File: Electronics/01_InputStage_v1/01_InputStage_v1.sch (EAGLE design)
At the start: 32 parts, among them J1 BARRIER_BLOCK-2PIN, J17 CONN_2X3_SMD, J2 BARRIER_BLOCK-2PIN, J3 BARRIER_BLOCK-2PIN, SW1 SWITCH_TABSSWITCH_TABS3, U1 XL4005-DEV, U2 DIODE_BIG

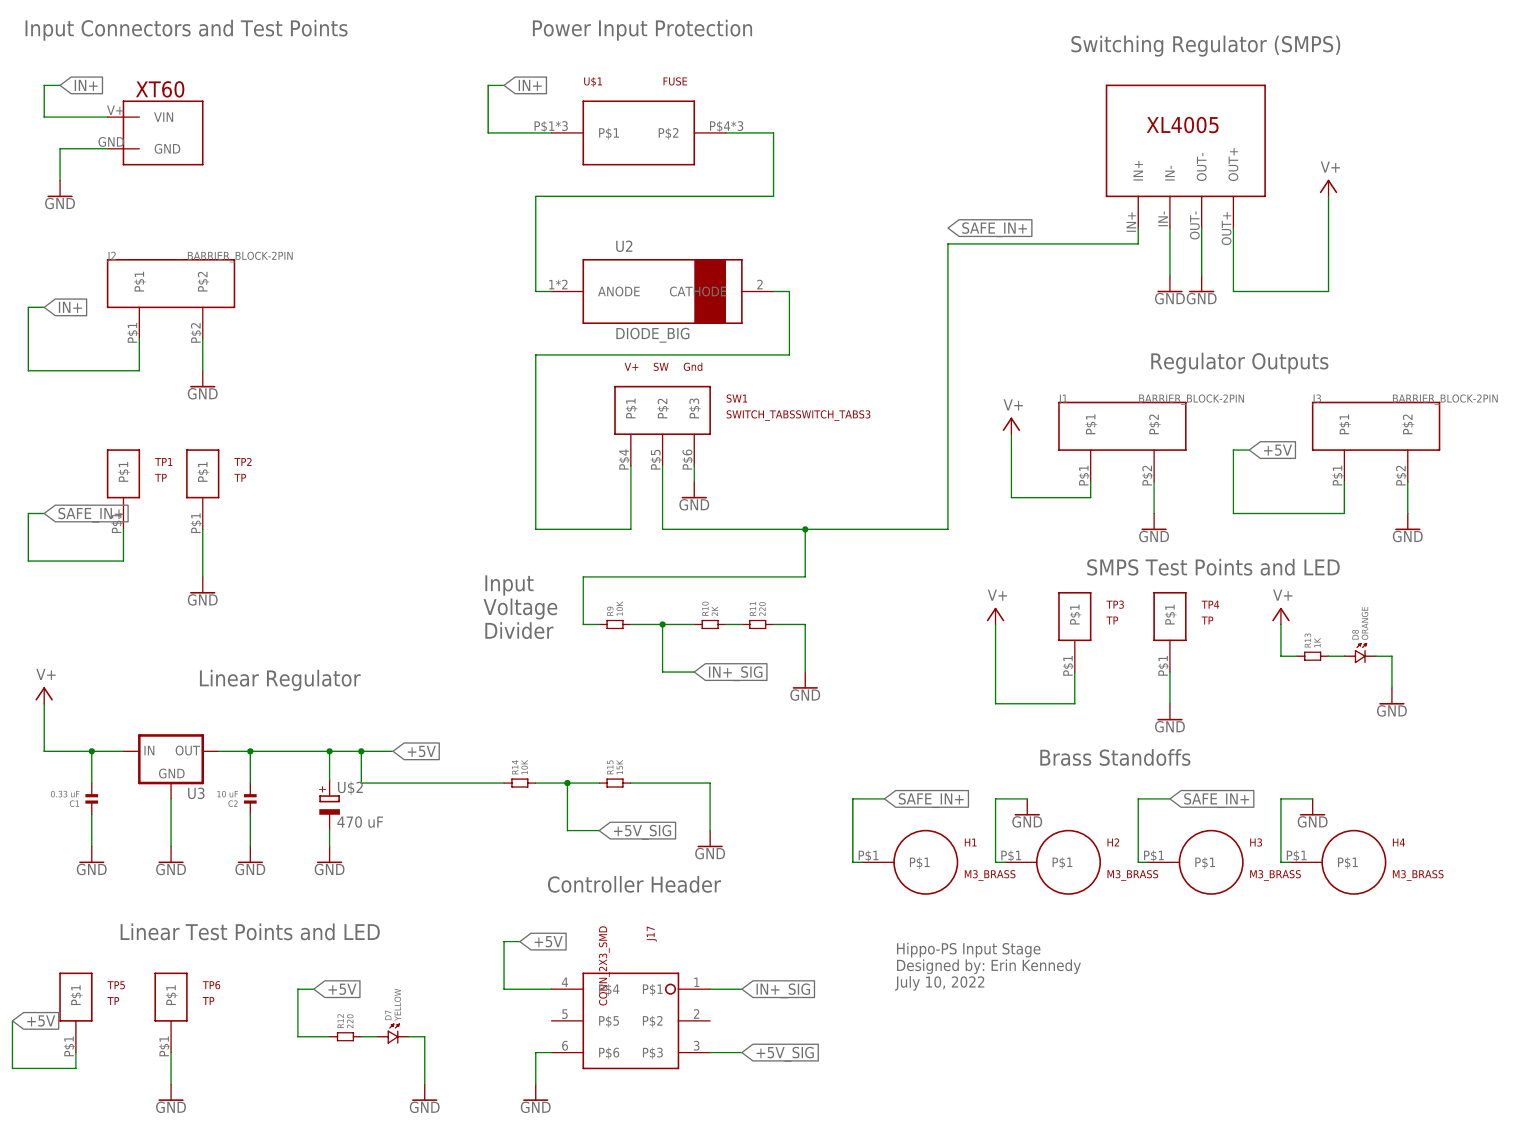
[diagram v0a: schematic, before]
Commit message: Input stage: Added PTC and moved some traces around
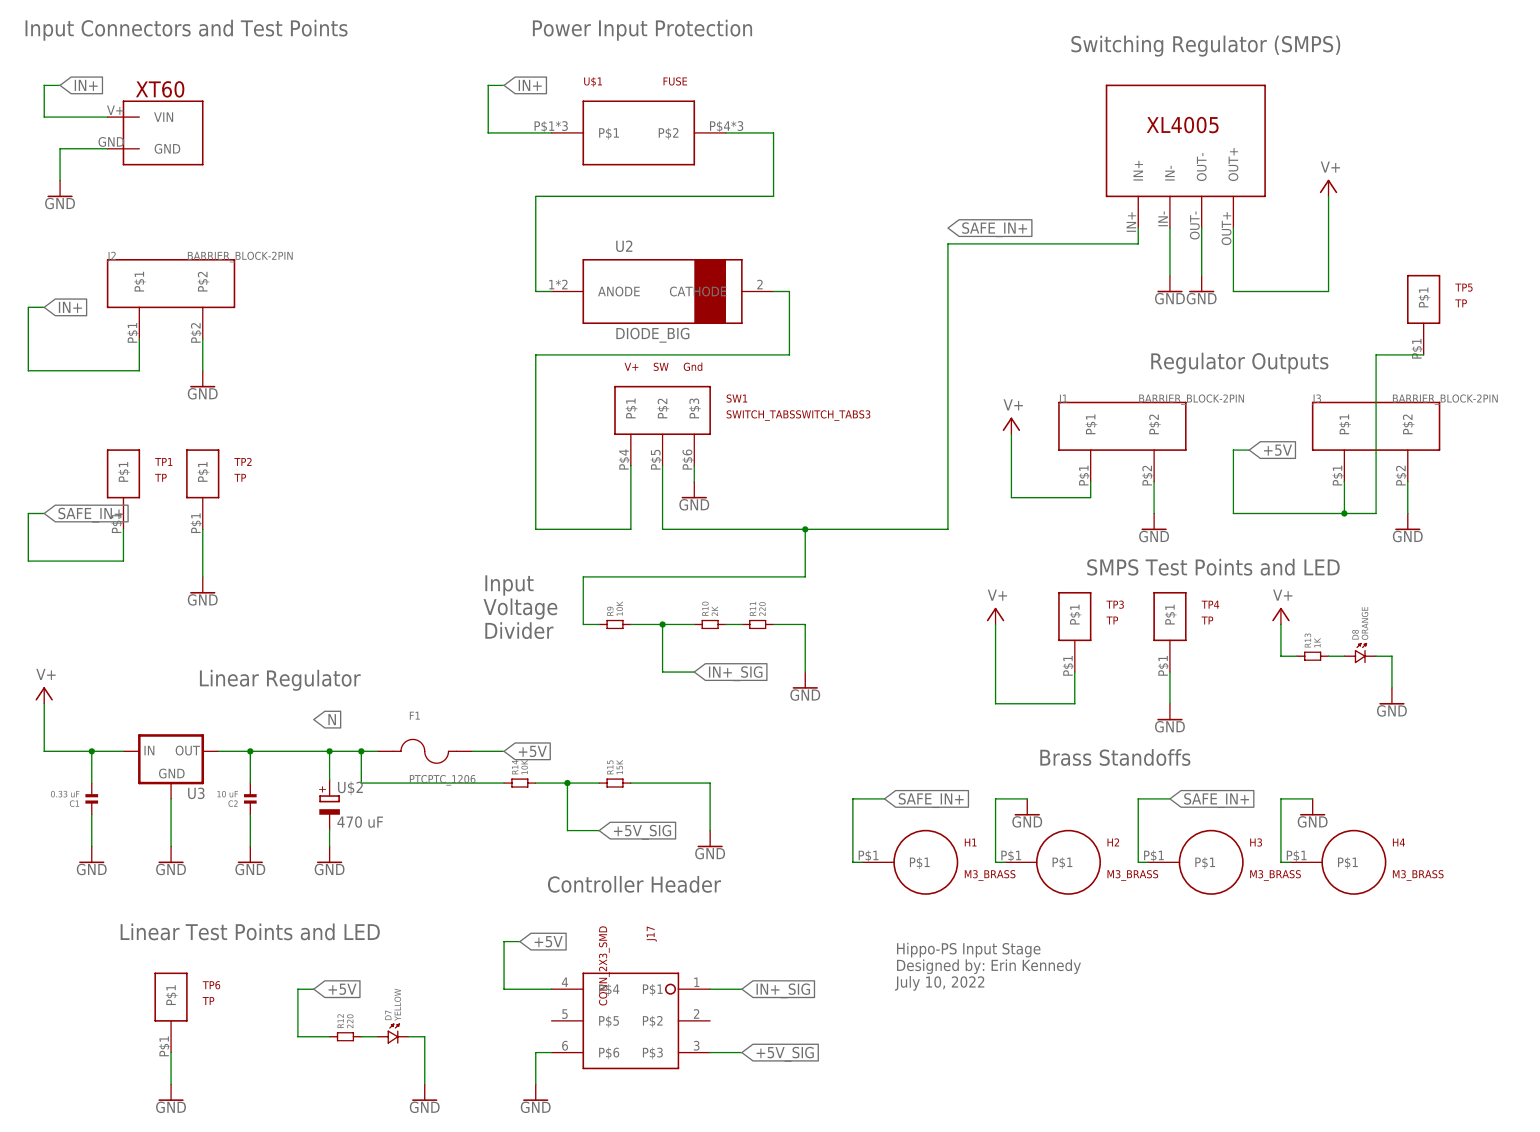
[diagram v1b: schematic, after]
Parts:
- added F1: PTCPTC_1206, Hippo-PS:PTCPTC_1206
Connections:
- new net N: C2.2, F1.1, R14.1, U$2.+, U3.OUT
- net +5V: now also F1.2; no longer C2.2, R14.1, U$2.+, U3.OUT
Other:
- moved on the sheet: TP5
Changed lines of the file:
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@@
 <part name="J3" library="Hippo-PS" deviceset="BARRIER_BLOCK-2PIN" device=""/>
 <part name="GND21" library="SparkFun-PowerSymbols" library_urn="urn:adsk.eagle:library:530" deviceset="GND" device=""/>
+<part name="F1" library="Hippo-PS" deviceset="PTC" device="PTC_1206"/>
 </parts>
 <sheets>
@@
 <attribute name="VALUE" x="218.44" y="53.086" size="1.778" layer="96" align="top-center"/>
 </instance>
-<instance part="TP5" gate="G$1" x="20.32" y="20.32" smashed="yes">
-<attribute name="NAME" x="25.4" y="25.4" size="1.27" layer="94"/>
-<attribute name="VALUE" x="25.4" y="22.86" size="1.27" layer="94"/>
+<instance part="TP5" gate="G$1" x="236.22" y="132.08" smashed="yes">
+<attribute name="NAME" x="241.3" y="137.16" size="1.27" layer="94"/>
+<attribute name="VALUE" x="241.3" y="134.62" size="1.27" layer="94"/>
 </instance>
 <instance part="TP6" gate="G$1" x="35.56" y="20.32" smashed="yes">
@@
 <instance part="GND21" gate="1" x="233.68" y="99.06" smashed="yes">
 <attribute name="VALUE" x="233.68" y="98.806" size="1.778" layer="96" align="top-center"/>
+</instance>
+<instance part="F1" gate="G$1" x="76.2" y="63.5" smashed="yes">
+<attribute name="NAME" x="73.66" y="68.58" size="1.27" layer="95"/>
+<attribute name="VALUE" x="73.66" y="58.42" size="1.27" layer="96"/>
 </instance>
 </instances>
@@
 <net name="+5V" class="0">
 <segment>
-<pinref part="U3" gate="G$1" pin="OUT"/>
-<wire x1="43.18" y1="63.5" x2="48.26" y2="63.5" width="0.1524" layer="91"/>
-<pinref part="C2" gate="G$1" pin="2"/>
-<wire x1="48.26" y1="63.5" x2="60.96" y2="63.5" width="0.1524" layer="91"/>
-<wire x1="48.26" y1="58.42" x2="48.26" y2="63.5" width="0.1524" layer="91"/>
-<junction x="48.26" y="63.5"/>
-<pinref part="U$2" gate="G$1" pin="+"/>
-<wire x1="60.96" y1="58.88" x2="60.96" y2="63.5" width="0.1524" layer="91"/>
-<junction x="60.96" y="63.5"/>
-<label x="71.12" y="63.5" size="1.778" layer="95" xref="yes"/>
-<wire x1="60.96" y1="63.5" x2="66.04" y2="63.5" width="0.1524" layer="91"/>
-<wire x1="66.04" y1="63.5" x2="71.12" y2="63.5" width="0.1524" layer="91"/>
-<wire x1="66.04" y1="63.5" x2="66.04" y2="58.42" width="0.1524" layer="91"/>
-<junction x="66.04" y="63.5"/>
-<pinref part="R14" gate="G$1" pin="1"/>
-<wire x1="66.04" y1="58.42" x2="88.9" y2="58.42" width="0.1524" layer="91"/>
-</segment>
-<segment>
-<pinref part="TP5" gate="G$1" pin="P$1"/>
-<wire x1="20.32" y1="15.24" x2="20.32" y2="12.7" width="0.1524" layer="91"/>
-<wire x1="20.32" y1="12.7" x2="10.16" y2="12.7" width="0.1524" layer="91"/>
-<wire x1="10.16" y1="12.7" x2="10.16" y2="20.32" width="0.1524" layer="91"/>
-<label x="10.16" y="20.32" size="1.778" layer="95" xref="yes"/>
-</segment>
-<segment>
 <pinref part="R12" gate="G$1" pin="1"/>
 <wire x1="60.96" y1="17.78" x2="55.88" y2="17.78" width="0.1524" layer="91"/>
@@
 </segment>
 <segment>
-<pinref part="J3" gate="G$1" pin="P$1"/>
-<wire x1="223.52" y1="106.68" x2="223.52" y2="101.6" width="0.1524" layer="91"/>
-<wire x1="223.52" y1="101.6" x2="205.74" y2="101.6" width="0.1524" layer="91"/>
 <wire x1="205.74" y1="101.6" x2="205.74" y2="111.76" width="0.1524" layer="91"/>
 <wire x1="205.74" y1="111.76" x2="208.28" y2="111.76" width="0.1524" layer="91"/>
 <label x="208.28" y="111.76" size="1.778" layer="95" xref="yes"/>
+<pinref part="J3" gate="G$1" pin="P$1"/>
+<wire x1="223.52" y1="106.68" x2="223.52" y2="101.6" width="0.1524" layer="91"/>
+<pinref part="TP5" gate="G$1" pin="P$1"/>
+<wire x1="236.22" y1="127" x2="228.6" y2="127" width="0.1524" layer="91"/>
+<wire x1="228.6" y1="127" x2="228.6" y2="101.6" width="0.1524" layer="91"/>
+<wire x1="228.6" y1="101.6" x2="223.52" y2="101.6" width="0.1524" layer="91"/>
+<junction x="223.52" y="101.6"/>
+<wire x1="205.74" y1="101.6" x2="223.52" y2="101.6" width="0.1524" layer="91"/>
+</segment>
+<segment>
+<pinref part="F1" gate="G$1" pin="2"/>
+<wire x1="83.82" y1="63.5" x2="88.9" y2="63.5" width="0.1524" layer="91"/>
+<label x="88.9" y="63.5" size="1.778" layer="95" xref="yes"/>
 </segment>
 </net>
@@
 </segment>
 </net>
+<net name="N" class="0">
+<segment>
+<pinref part="U3" gate="G$1" pin="OUT"/>
+<wire x1="43.18" y1="63.5" x2="48.26" y2="63.5" width="0.1524" layer="91"/>
+<pinref part="C2" gate="G$1" pin="2"/>
+<wire x1="48.26" y1="63.5" x2="60.96" y2="63.5" width="0.1524" layer="91"/>
+<wire x1="48.26" y1="58.42" x2="48.26" y2="63.5" width="0.1524" layer="91"/>
+<junction x="48.26" y="63.5"/>
+<pinref part="U$2" gate="G$1" pin="+"/>
+<wire x1="60.96" y1="58.88" x2="60.96" y2="63.5" width="0.1524" layer="91"/>
+<junction x="60.96" y="63.5"/>
+<wire x1="60.96" y1="63.5" x2="66.04" y2="63.5" width="0.1524" layer="91"/>
+<wire x1="66.04" y1="63.5" x2="66.04" y2="58.42" width="0.1524" layer="91"/>
+<pinref part="R14" gate="G$1" pin="1"/>
+<wire x1="66.04" y1="58.42" x2="88.9" y2="58.42" width="0.1524" layer="91"/>
+<pinref part="F1" gate="G$1" pin="1"/>
+<wire x1="68.58" y1="63.5" x2="66.04" y2="63.5" width="0.1524" layer="91"/>
+<junction x="66.04" y="63.5"/>
+<label x="58.42" y="68.58" size="1.778" layer="95" xref="yes"/>
+</segment>
+</net>

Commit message: Change fuse holder to through-hole component
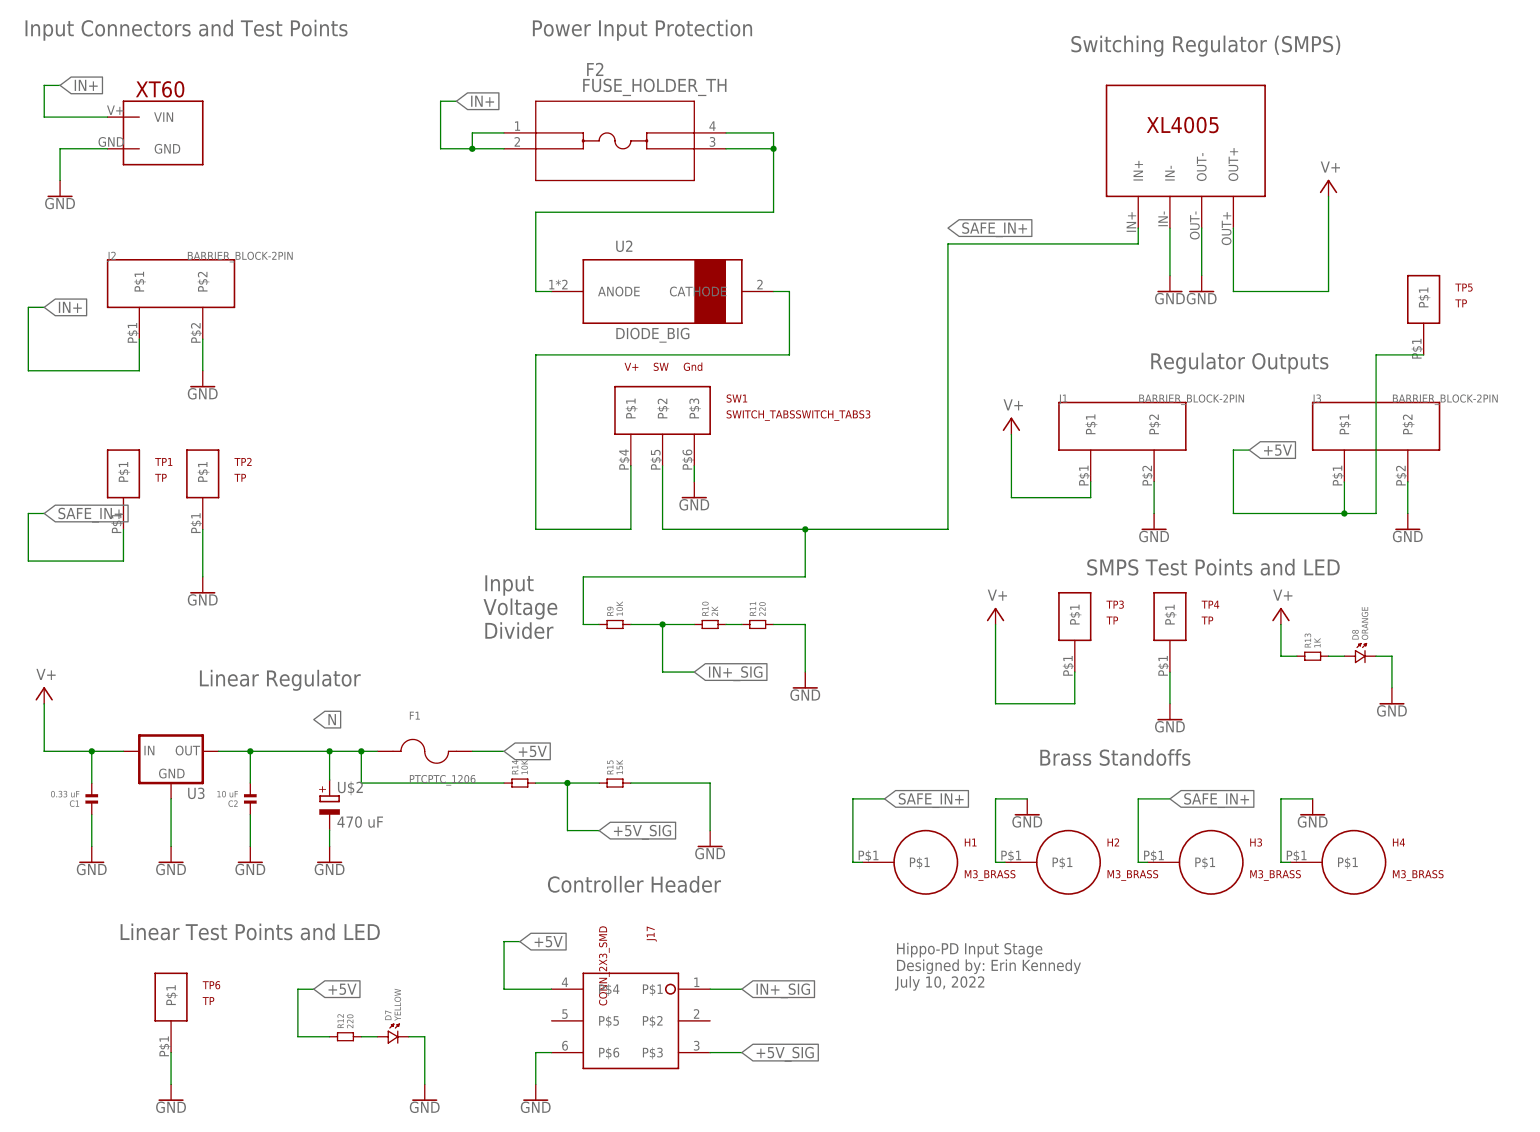
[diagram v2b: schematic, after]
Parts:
- removed U$1: FUSE, Hippo-PS:FUSE
- added F2: FUSE_HOLDER_TH, Hippo-PS:FUSE_HOLDER_TH
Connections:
- net IN+: now also F2.1, F2.2; no longer U$1.P$1
- net N$1: now also F2.3, F2.4; no longer U$1.P$2
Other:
- note added: "Hippo-PD Input Stage Designed by: Erin Kennedy July 10, 2022"
- note removed: "Hippo-PS Input Stage Designed by: Erin Kennedy July 10, 2022"
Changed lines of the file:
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@@
 <part name="H4" library="Hippo-PS" deviceset="M3_BRASS" device=""/>
 <part name="U$5" library="Hippo-PS" deviceset="XT60" device=""/>
-<part name="U$1" library="Hippo-PS" deviceset="FUSE" device=""/>
 <part name="TP1" library="Hippo-PS" deviceset="TP" device=""/>
 <part name="TP2" library="Hippo-PS" deviceset="TP" device=""/>
@@
 <part name="GND21" library="SparkFun-PowerSymbols" library_urn="urn:adsk.eagle:library:530" deviceset="GND" device=""/>
 <part name="F1" library="Hippo-PS" deviceset="PTC" device="PTC_1206"/>
+<part name="F2" library="Hippo-PS" deviceset="FUSE_HOLDER_TH" device=""/>
 </parts>
 <sheets>
 <sheet>
 <plain>
-<text x="151.638" y="25.654" size="1.778" layer="95">Hippo-PS Input Stage
+<text x="151.638" y="25.654" size="1.778" layer="95">Hippo-PD Input Stage
 Designed by: Erin Kennedy
 July 10, 2022 </text>
@@
 </instance>
 <instance part="U$5" gate="G$1" x="30.48" y="162.56" smashed="yes"/>
-<instance part="U$1" gate="G$1" x="111.76" y="162.56" smashed="yes">
-<attribute name="NAME" x="101.6" y="170.18" size="1.27" layer="94"/>
-<attribute name="VALUE" x="114.3" y="170.18" size="1.27" layer="94"/>
-</instance>
 <instance part="TP1" gate="G$1" x="27.94" y="104.14" smashed="yes">
 <attribute name="NAME" x="33.02" y="109.22" size="1.27" layer="94"/>
@@
 <attribute name="NAME" x="73.66" y="68.58" size="1.27" layer="95"/>
 <attribute name="VALUE" x="73.66" y="58.42" size="1.27" layer="96"/>
+</instance>
+<instance part="F2" gate="A" x="86.36" y="162.56" smashed="yes">
+<attribute name="NAME" x="101.9556" y="171.6786" size="2.0828" layer="95" ratio="6" rot="SR0"/>
+<attribute name="VALUE" x="101.3206" y="169.1386" size="2.0828" layer="96" ratio="6" rot="SR0"/>
 </instance>
 </instances>
@@
 </segment>
 <segment>
-<pinref part="U$1" gate="G$1" pin="P$1"/>
-<wire x1="96.52" y1="162.56" x2="86.36" y2="162.56" width="0.1524" layer="91"/>
-<wire x1="86.36" y1="162.56" x2="86.36" y2="170.18" width="0.1524" layer="91"/>
-<wire x1="86.36" y1="170.18" x2="88.9" y2="170.18" width="0.1524" layer="91"/>
-<label x="88.9" y="170.18" size="1.778" layer="95" xref="yes"/>
+<wire x1="88.9" y1="160.02" x2="83.82" y2="160.02" width="0.1524" layer="91"/>
+<wire x1="83.82" y1="160.02" x2="78.74" y2="160.02" width="0.1524" layer="91"/>
+<wire x1="78.74" y1="160.02" x2="78.74" y2="167.64" width="0.1524" layer="91"/>
+<wire x1="78.74" y1="167.64" x2="81.28" y2="167.64" width="0.1524" layer="91"/>
+<label x="81.28" y="167.64" size="1.778" layer="95" xref="yes"/>
+<pinref part="F2" gate="A" pin="2"/>
+<pinref part="F2" gate="A" pin="1"/>
+<wire x1="88.9" y1="162.56" x2="83.82" y2="162.56" width="0.1524" layer="91"/>
+<wire x1="83.82" y1="162.56" x2="83.82" y2="160.02" width="0.1524" layer="91"/>
+<junction x="83.82" y="160.02"/>
 </segment>
 </net>
@@
 <net name="N$1" class="0">
 <segment>
-<pinref part="U$1" gate="G$1" pin="P$2"/>
-<wire x1="124.46" y1="162.56" x2="132.08" y2="162.56" width="0.1524" layer="91"/>
-<wire x1="132.08" y1="162.56" x2="132.08" y2="152.4" width="0.1524" layer="91"/>
-<wire x1="132.08" y1="152.4" x2="93.98" y2="152.4" width="0.1524" layer="91"/>
-<wire x1="93.98" y1="152.4" x2="93.98" y2="137.16" width="0.1524" layer="91"/>
+<wire x1="124.46" y1="160.02" x2="132.08" y2="160.02" width="0.1524" layer="91"/>
+<wire x1="132.08" y1="160.02" x2="132.08" y2="149.86" width="0.1524" layer="91"/>
+<wire x1="132.08" y1="149.86" x2="93.98" y2="149.86" width="0.1524" layer="91"/>
+<wire x1="93.98" y1="149.86" x2="93.98" y2="137.16" width="0.1524" layer="91"/>
 <pinref part="U2" gate="G$1" pin="ANODE"/>
 <wire x1="93.98" y1="137.16" x2="96.52" y2="137.16" width="0.1524" layer="91"/>
+<pinref part="F2" gate="A" pin="3"/>
+<pinref part="F2" gate="A" pin="4"/>
+<wire x1="124.46" y1="162.56" x2="132.08" y2="162.56" width="0.1524" layer="91"/>
+<wire x1="132.08" y1="162.56" x2="132.08" y2="160.02" width="0.1524" layer="91"/>
+<junction x="132.08" y="160.02"/>
 </segment>
 </net>
